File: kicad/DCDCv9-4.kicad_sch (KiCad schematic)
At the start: 198 parts, among them J1 43650-0315, J1.1 43645-0300, J1.2 Conn_01x01_Pin, J1.3 Conn_01x01_Pin, J1.4 Conn_01x01_Pin, J2 Conn_01x02_Male, J3 Conn_01x02, J3.1 Conn_01x02, J3.2 Conn_01x01_Pin, J3.3 Conn_01x01_Pin, J4 Conn_01x02_Male, J5 XT60 Male, J5.1 XT60 Female (wrong symbol ik), J6 Conn_01x02_Male, J7 Conn_01x02_Male, J8 Conn_01x02_Male, M1 Fan, Q1 PMV20ENR, Q10 IMBG120R026M2HXTMA1, Q11 IMBG120R026M2HXTMA1, Q2 PMV20ENR, Q3 SIHP24N80AE-GE3, Q4 IXYP8N90C3, Q5 PMV20ENR, Q6 PMV20ENR, Q7 PMV20ENR, T1 DIY Transformer ETD 39, T1.1 Ferrite Core, T1.2 Ferrite Core (gapped), T1.3 1800 mm 120 x 0.1 mm HF litz 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, T1.4 165 mm 600 x 0,071 mm HF litz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, T1.5 165 mm 600 x 0,071 mm HF litz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, U1 RP-1215S, U10 LM2904BIDDFR, U11 2EDR8259XXUMA1, U12 UCC25600, U13 ZXRE330ASA-7, U14 LM2904BIDDFR, U2 RT9058-90GVL, U3 MP4541_SOP8-EP, U4 TLV61048DBVR, U6 LM2904BIDDFR, U7 TL431BCDBZR, U9 ACPL-217-50AE

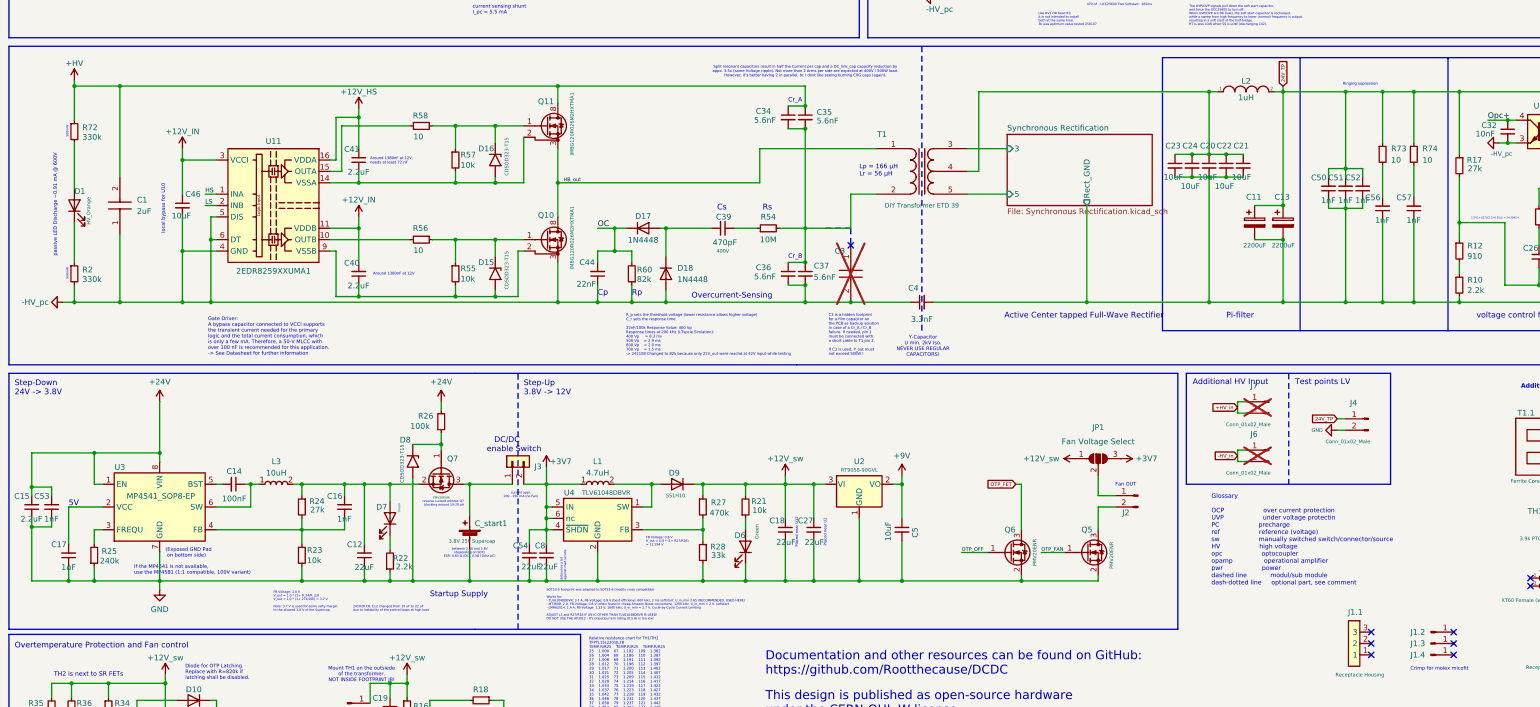
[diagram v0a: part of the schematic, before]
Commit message: Added ferrite bead to U3, enlarged SR FET cooling surface
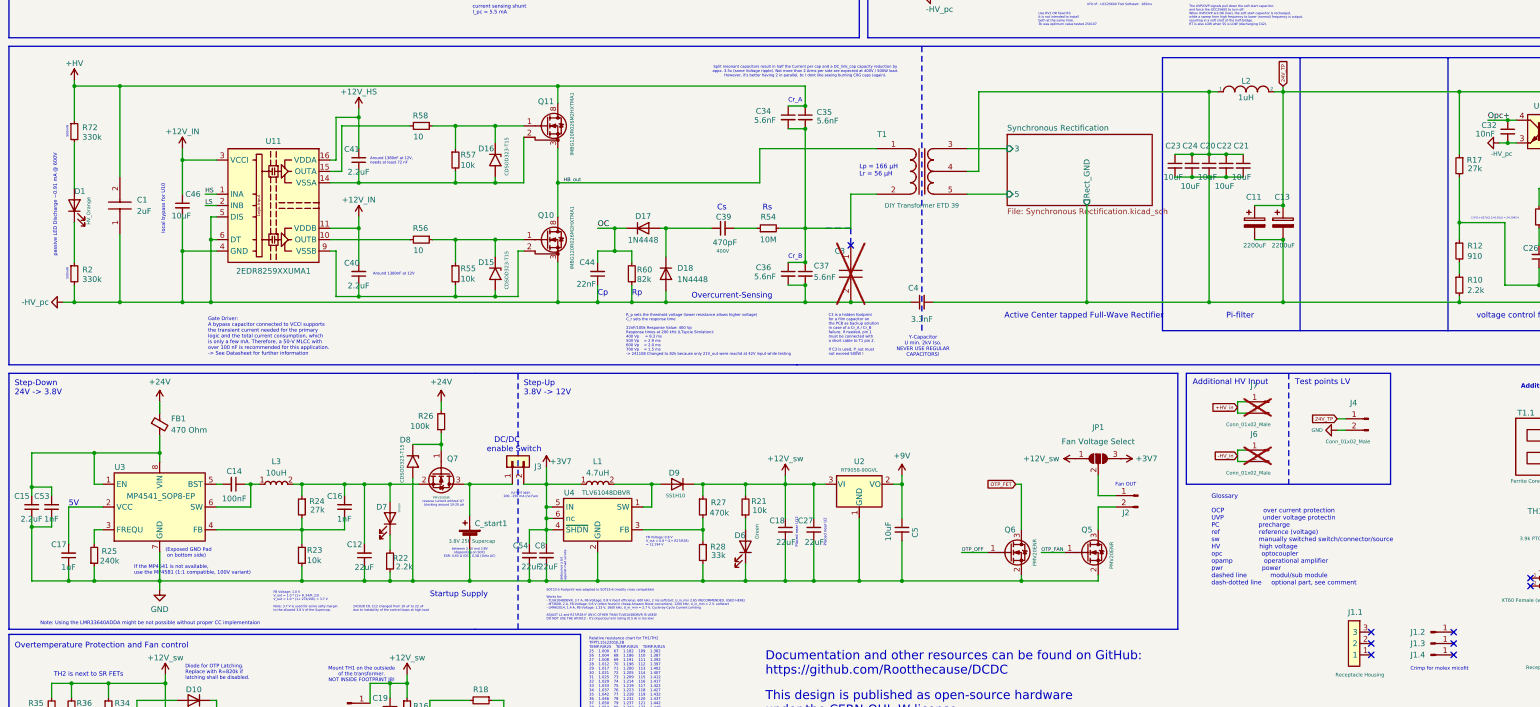
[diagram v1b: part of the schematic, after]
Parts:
- removed C50, C51, C52, C56, C57: 1nF, DCDC-Footprints:C_0603_1608Metric, symbol Device:C_Small
- removed R73, R74: 10, DCDC-Footprints:R_0603_1608Metric, symbol Device:R_Small
- added FB1: 470 Ohm, Inductor_SMD:L_0603_1608Metric, symbol Device:FerriteBead_Small
- JP1: now left out of the parts list
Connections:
- net +24V: now also FB1.1; no longer C15.2, C53.2, U3.1 (EN), U3.8 (VIN)
- new net: C15.2, C53.2, FB1.2, U3.1 (EN), U3.8 (VIN)
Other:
- note added: "Note: Using the LMR33640ADDA might be not possible without proper CC implementaion"
- note removed: "Ringing supression"
- title: DC/DC v9-3r1.4 -> DC/DC v9-4r0.1

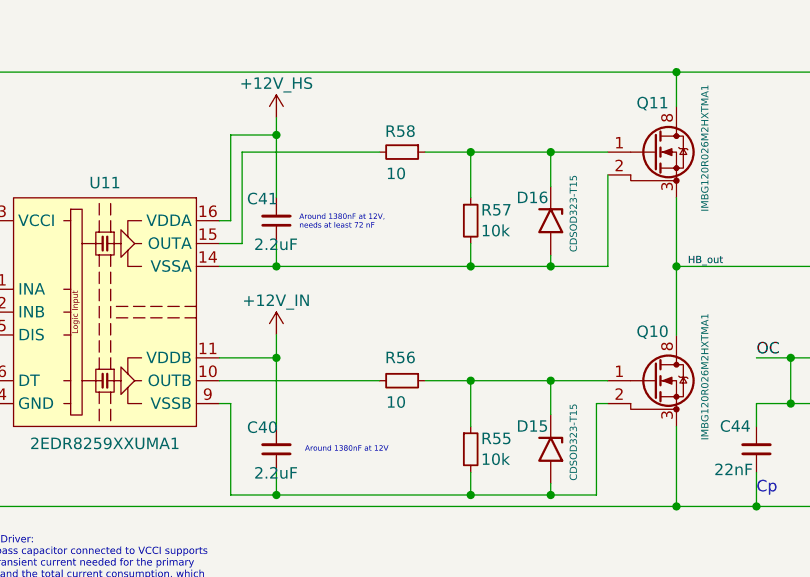
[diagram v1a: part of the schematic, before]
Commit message: added PCBA BOM, added lots of JLC part numbers
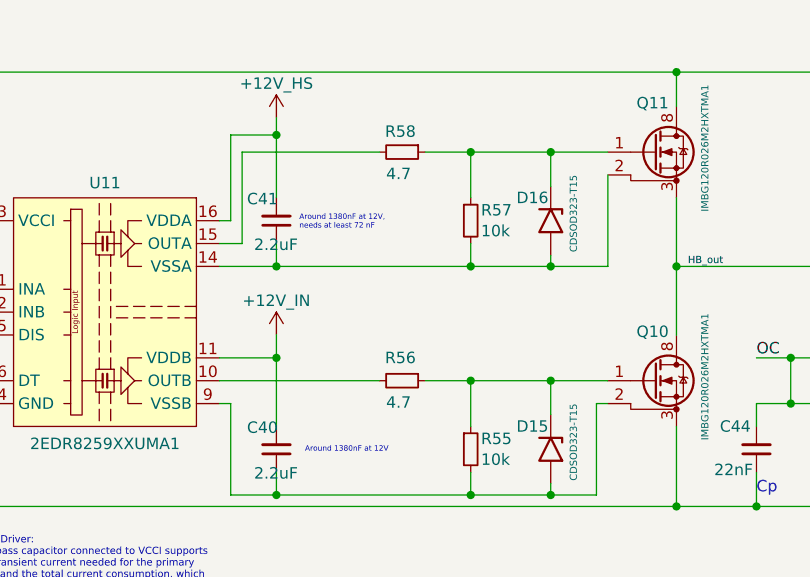
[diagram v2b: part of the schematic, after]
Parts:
- C1: JLCPCB Part # (none) -> C3794423
- C11, C13: JLCPCB Part # (none) -> C136285
- C12, C18, C27, C42, C54, C8: JLCPCB Part # (none) -> C45783
- C14, C28: JLCPCB Part # (none) -> C14663
- C15, C2, C40, C41: JLCPCB Part # (none) -> C377773
- C16, C49, C53, C55: JLCPCB Part # (none) -> C1588
- C17, C19, C45: JLCPCB Part # (none) -> C15849
- C20, C21, C22, C23, C24: JLCPCB Part # (none) -> C703129
- C26, C44, C47: JLCPCB Part # (none) -> C21122
- C29: JLCPCB Part # (none) -> C1671
- C30, C32, C48: JLCPCB Part # (none) -> C57112
- C33, C46, C5: JLCPCB Part # (none) -> C440198
- C39: JLCPCB Part # (none) -> C22440592; Manufacturer_Part_Number 885342208005 -> VJ1206A471JXGTW1HV
- C4: JLCPCB Part # (none) -> C1620958
- C43: JLCPCB Part # (none) -> C1623
- C_start1: JLCPCB Part # (none) -> C4550878
- D1: JLCPCB Part # (none) -> C375578
- D10, D17, D18, D2: JLCPCB Part # (none) -> C526203
- D11, D12: JLCPCB Part # (none) -> C24643891
- D13, D3, D4, D5, D6, D7, D9: JLCPCB Part # (none) -> C497917
- D14: JLCPCB Part # (none) -> C46613027
- D15, D16, D8: JLCPCB Part # (none) -> C1517910
- F1: JLCPCB Part # (none) -> C720204
- F1.1, F1.2: JLCPCB Part # (none) -> C206901
- FB1: JLCPCB Part # (none) -> C5279032; Manufacturer_Part_Number (none) -> 742792645
- J1: JLCPCB Part # (none) -> C293546
- L1: JLCPCB Part # (none) -> C3224051
- L2: JLCPCB Part # (none) -> C6464476
- L3: JLCPCB Part # (none) -> C2050513
- Q1, Q2, Q5, Q6, Q7: JLCPCB Part # (none) -> C456088
- Q10, Q11: JLCPCB Part # (none) -> IMBG120R026M2HXTMA1
- Q4: JLCPCB Part # (none) -> C17247224
- R1, R71: JLCPCB Part # (none) -> C2089706
- R2, R72: JLCPCB Part # (none) -> C414825
- R35: JLCPCB Part # (none) -> C23137
- R54: JLCPCB Part # (none) -> C2078633
- R56, R58: value 10 -> 4.7; JLCPCB Part # (none) -> C313986; Manufacturer_Part_Number RC1206FR-7W10RL -> ERJ-P08J4R7V
- RV1: JLCPCB Part # (none) -> C6149942
- RV2: JLCPCB Part # (none) -> C5273013
- TH2: JLCPCB Part # (none) -> C2655286
- U10, U14, U6: JLCPCB Part # (none) -> C4366469
- U11: JLCPCB Part # (none) -> C17455725
- U12: JLCPCB Part # (none) -> C130223
- U13: JLCPCB Part # (none) -> C461150
- U3: JLCPCB Part # (none) -> C3192953
- U4: JLCPCB Part # (none) -> C2861467
- U7: JLCPCB Part # (none) -> C6971
- U9: JLCPCB Part # (none) -> C5157608
